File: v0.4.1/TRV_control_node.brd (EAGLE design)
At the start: 65 x 30.7 mm, 45 parts, among them J3 AMP FCI 10103594-0001LF, J4 455-1750-1-ND, J6 AMP FCI 10103594-0001LF, SW1 EVQQ, SW2 EVQQ, U1 PCA9306, U11 915MHz, U2 FT231XQ-R, U5 ATMEGA328P-MU, U8 MCP1703/3.3V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

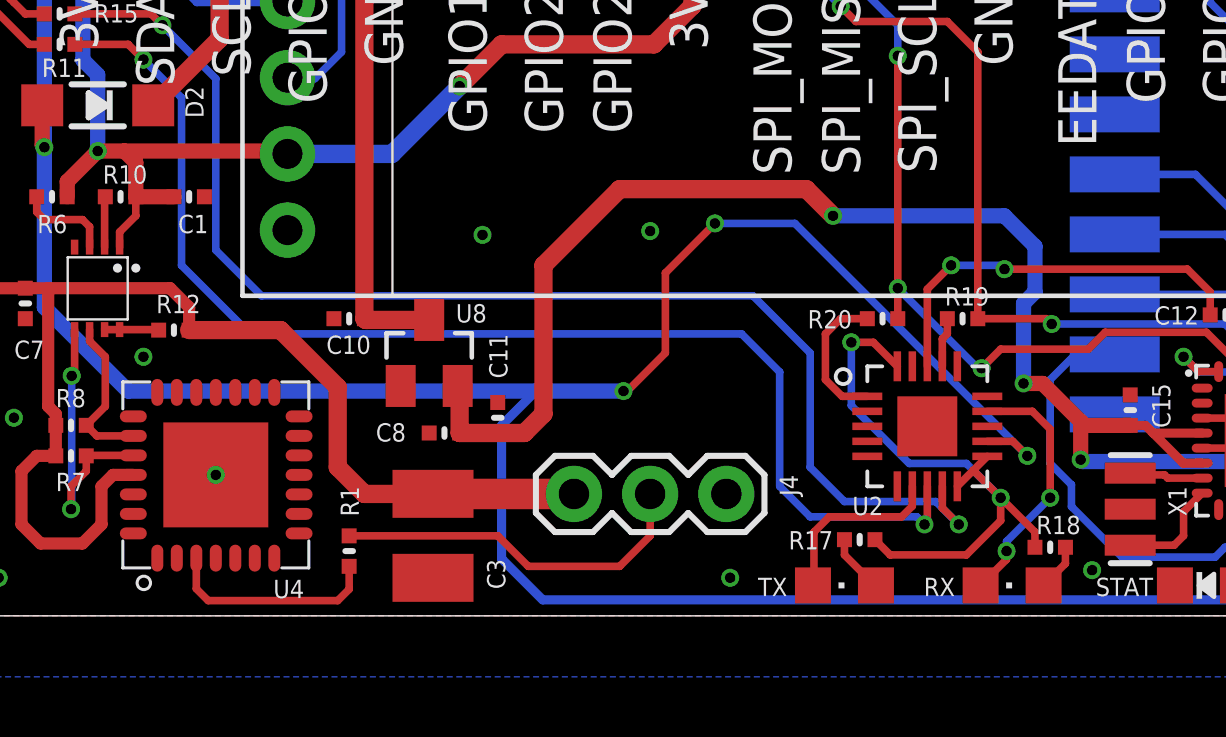
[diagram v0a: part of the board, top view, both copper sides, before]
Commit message: vreg adjustment
Moved the Vreg and its caps a bit away from the 3 pin servo header
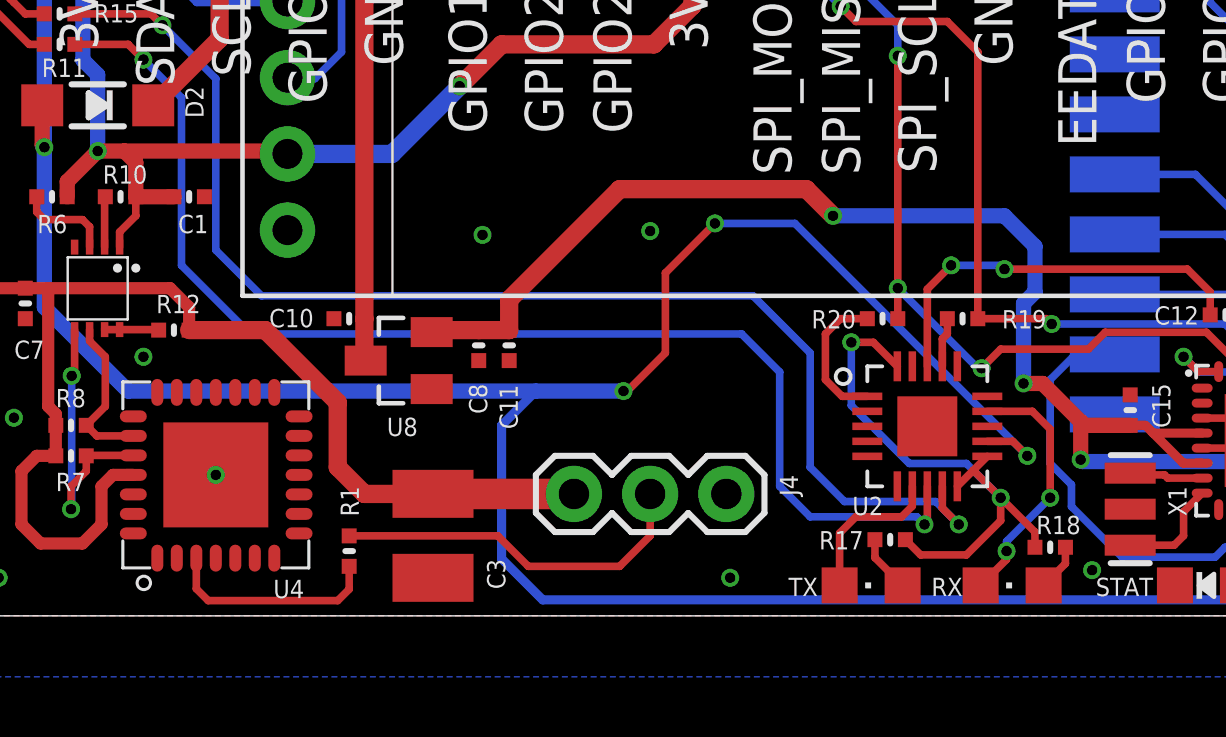
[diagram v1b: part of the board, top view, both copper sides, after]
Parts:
- moved C8 3.14 mm to (21.6, 9.02), turned to 90 degrees
- moved C11 2.44 mm to (22.6, 9.02), turned to 90 degrees
- moved U8 1.05 mm to (18.9, 8.51), turned to 90 degrees
- moved R17 1.02 mm to (35.3, 2.54)
- moved TX 0.89 mm to (34.7, 1.02)
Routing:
- net VCC: track 97.6 -> 93.3 mm
- net FTDI_3.3V: track 20.7 -> 19.7 mm
- net N$18: track 6.09 -> 5.20 mm
- net VIN: track 24.9 -> 24.1 mm
